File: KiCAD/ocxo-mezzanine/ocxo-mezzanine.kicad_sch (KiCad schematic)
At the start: 35 parts, among them J1 Conn_01x12_Pin, J2 lownoise-LDO, U1 DAC8563SDGSR, U2 Si8641BA-B-IU, U3 OPA192IDBVR, U6 LDL1117S50R_, X1 OSC5A2B02

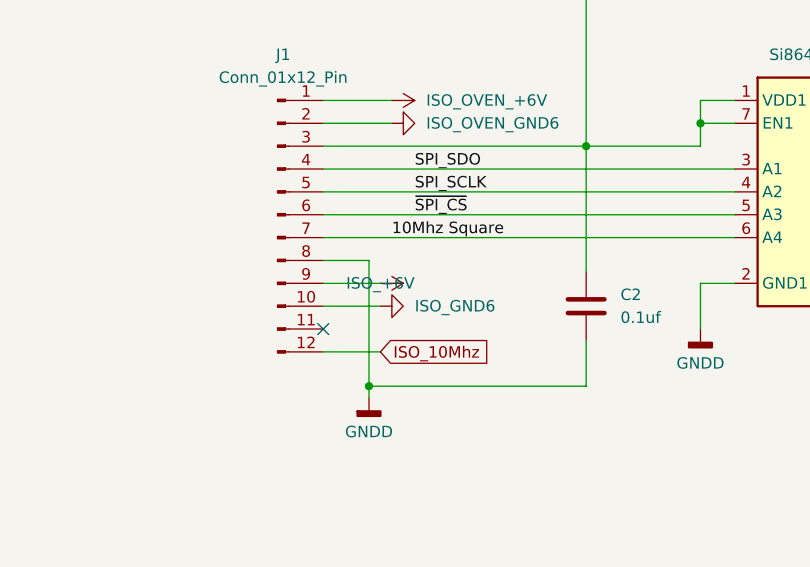
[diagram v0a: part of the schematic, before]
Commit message: Reworked, now with IRIG option board complete
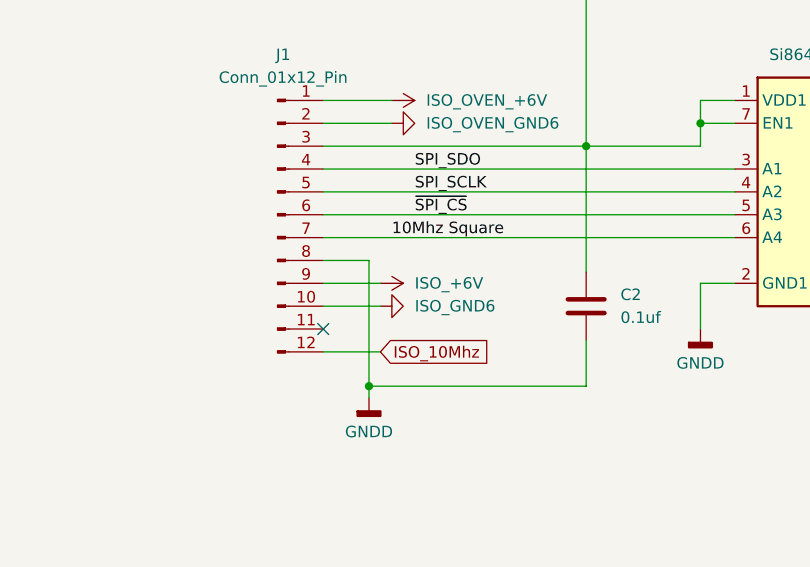
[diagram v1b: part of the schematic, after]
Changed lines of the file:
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@@
 		)
 		(property "Value" "ISO_+6V"
-			(at 111.76 92.7099 90)
+			(at 119.38 92.71 90)
 			(effects
 				(font
